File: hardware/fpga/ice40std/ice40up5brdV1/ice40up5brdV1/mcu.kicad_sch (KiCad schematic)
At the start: 10 parts, among them J3 Conn_01x06_Male, J4 Conn_01x04_Male, U5 ATSAMD11D14A-M

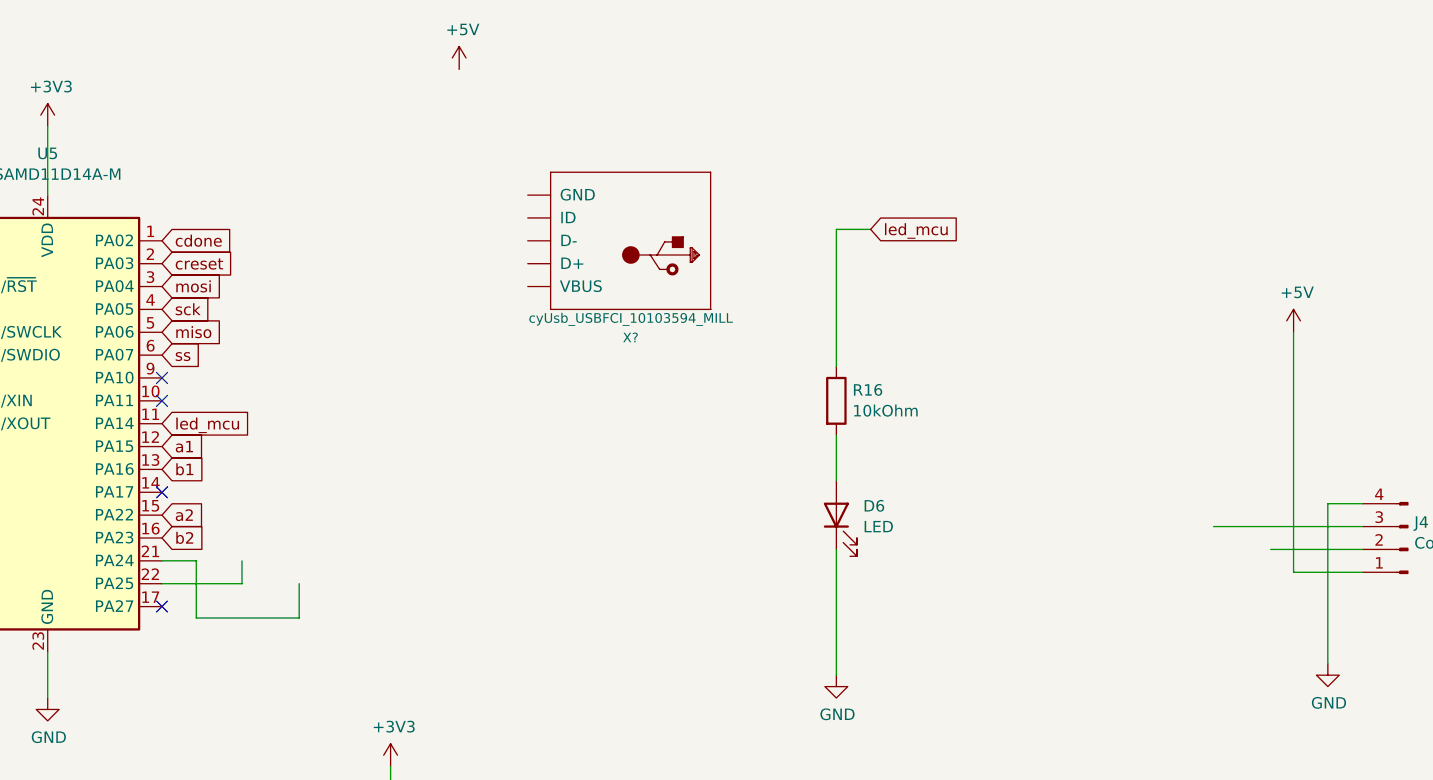
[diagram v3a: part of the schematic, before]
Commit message: started linear regs / Amphenol USB
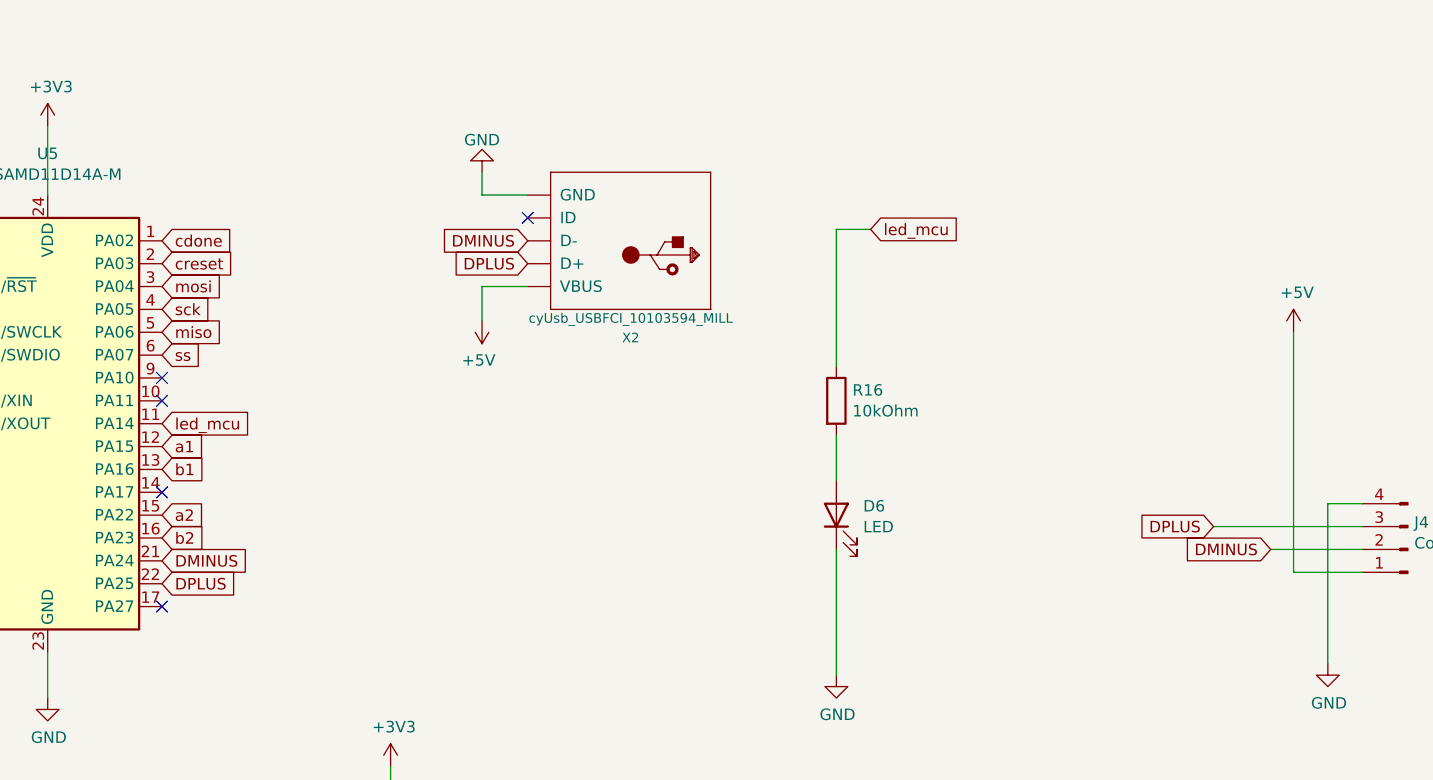
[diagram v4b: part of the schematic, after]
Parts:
- gave numbers to parts that had none: 1
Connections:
- net +5V: now also X2.VBUS
- net GND: now also X2.BASE@1 (GND), X2.BASE@2 (GND), X2.GND, X2.SPRT@1 (GND), X2.SPRT@2 (GND), X2.SPRT@3 (GND), X2.SPRT@4 (GND)
- net DMINUS: now reaches U5.21 (PA24)
- net DMINUS: now also J4.2 (Pin_2), X2.D-
- net DPLUS: now reaches U5.22 (PA25)
- net DPLUS: now also J4.3 (Pin_3), X2.D+
- no-connect marks 4 -> 5
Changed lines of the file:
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@@
   (no_connect (at 88.9 55.88))
   (no_connect (at 88.9 81.28))
+  (no_connect (at 129.54 38.1))
   (wire (pts (xy 106.68 102.87) (xy 114.3 102.87))
     (stroke (width 0) (type default) (color 0 0 0 0))
@@
     (stroke (width 0) (type default) (color 0 0 0 0))
   )
-  (wire (pts (xy 92.71 76.2) (xy 92.71 82.55))
-    (stroke (width 0) (type default) (color 0 0 0 0))
-  )
   (wire (pts (xy 33.02 71.12) (xy 33.02 80.01))
     (stroke (width 0) (type default) (color 0 0 0 0))
@@
     (stroke (width 0) (type default) (color 0 0 0 0))
   )
-  (wire (pts (xy 92.71 82.55) (xy 104.14 82.55))
-    (stroke (width 0) (type default) (color 0 0 0 0))
-  )
   (wire (pts (xy 33.02 58.42) (xy 33.02 63.5))
     (stroke (width 0) (type default) (color 0 0 0 0))
@@
     (stroke (width 0) (type default) (color 0 0 0 0))
   )
-  (wire (pts (xy 88.9 76.2) (xy 92.71 76.2))
+  (wire (pts (xy 124.46 45.72) (xy 129.54 45.72))
     (stroke (width 0) (type default) (color 0 0 0 0))
   )
@@
     (stroke (width 0) (type default) (color 0 0 0 0))
   )
-  (wire (pts (xy 97.79 78.74) (xy 97.79 76.2))
-    (stroke (width 0) (type default) (color 0 0 0 0))
-  )
   (wire (pts (xy 49.53 135.89) (xy 49.53 129.54))
     (stroke (width 0) (type default) (color 0 0 0 0))
@@
     (stroke (width 0) (type default) (color 0 0 0 0))
   )
+  (wire (pts (xy 124.46 33.02) (xy 124.46 35.56))
+    (stroke (width 0) (type default) (color 0 0 0 0))
+  )
+  (wire (pts (xy 124.46 35.56) (xy 129.54 35.56))
+    (stroke (width 0) (type default) (color 0 0 0 0))
+  )
   (wire (pts (xy 46.99 125.73) (xy 40.64 125.73))
     (stroke (width 0) (type default) (color 0 0 0 0))
@@
     (stroke (width 0) (type default) (color 0 0 0 0))
   )
-  (wire (pts (xy 104.14 82.55) (xy 104.14 78.74))
-    (stroke (width 0) (type default) (color 0 0 0 0))
-  )
   (wire (pts (xy 163.83 54.61) (xy 163.83 39.37))
     (stroke (width 0) (type default) (color 0 0 0 0))
   )
+  (wire (pts (xy 124.46 49.53) (xy 124.46 45.72))
+    (stroke (width 0) (type default) (color 0 0 0 0))
+  )
   (wire (pts (xy 27.94 33.02) (xy 29.21 33.02))
     (stroke (width 0) (type default) (color 0 0 0 0))
@@
     (stroke (width 0) (type default) (color 0 0 0 0))
   )
-  (wire (pts (xy 88.9 78.74) (xy 97.79 78.74))
-    (stroke (width 0) (type default) (color 0 0 0 0))
-  )
   (wire (pts (xy 120.65 102.87) (xy 120.65 106.68))
     (stroke (width 0) (type default) (color 0 0 0 0))
@@
     )
   )
+  (global_label "DPLUS" (shape input) (at 129.54 43.18 180) (fields_autoplaced)
+    (effects (font (size 1.27 1.27)) (justify right))
+    (property "Intersheet References" "${INTERSHEET_REFS}" (id 0) (at 121.1077 43.1006 0)
+      (effects (font (size 1.27 1.27)) (justify right) hide)
+    )
+  )
   (global_label "swd_clk" (shape input) (at 40.64 123.19 180) (fields_autoplaced)
     (effects (font (size 1.27 1.27)) (justify right))
@@
     )
   )
+  (global_label "DPLUS" (shape input) (at 205.74 72.39 180) (fields_autoplaced)
+    (effects (font (size 1.27 1.27)) (justify right))
+    (property "Intersheet References" "${INTERSHEET_REFS}" (id 0) (at 197.3077 72.3106 0)
+      (effects (font (size 1.27 1.27)) (justify right) hide)
+    )
+  )
+  (global_label "DMINUS" (shape input) (at 212.09 74.93 180) (fields_autoplaced)
+    (effects (font (size 1.27 1.27)) (justify right))
+    (property "Intersheet References" "${INTERSHEET_REFS}" (id 0) (at 202.5691 74.8506 0)
+      (effects (font (size 1.27 1.27)) (justify right) hide)
+    )
+  )
+  (global_label "DMINUS" (shape input) (at 129.54 40.64 180) (fields_autoplaced)
+    (effects (font (size 1.27 1.27)) (justify right))
+    (property "Intersheet References" "${INTERSHEET_REFS}" (id 0) (at 120.0191 40.5606 0)
+      (effects (font (size 1.27 1.27)) (justify right) hide)
+    )
+  )
   (global_label "b1" (shape input) (at 88.9 66.04 0) (fields_autoplaced)
     (effects (font (size 1.27 1.27)) (justify left))
@@
     )
   )
+  (global_label "DPLUS" (shape input) (at 88.9 78.74 0) (fields_autoplaced)
+    (effects (font (size 1.27 1.27)) (justify left))
+    (property "Intersheet References" "${INTERSHEET_REFS}" (id 0) (at 97.3323 78.8194 0)
+      (effects (font (size 1.27 1.27)) (justify left) hide)
+    )
+  )
   (global_label "led_mcu" (shape input) (at 167.64 39.37 0) (fields_autoplaced)
     (effects (font (size 1.27 1.27)) (justify left))
@@
     (property "Intersheet References" "${INTERSHEET_REFS}" (id 0) (at 0 0 0)
       (effects (font (size 1.27 1.27)) hide)
+    )
+  )
+  (global_label "DMINUS" (shape input) (at 88.9 76.2 0) (fields_autoplaced)
+    (effects (font (size 1.27 1.27)) (justify left))
+    (property "Intersheet References" "${INTERSHEET_REFS}" (id 0) (at 98.4209 76.2794 0)
+      (effects (font (size 1.27 1.27)) (justify left) hide)
     )
   )
@@
     (pin "4")
   )
-  (symbol (lib_id "power:+5V") (at 121.92 21.59 0) (unit 1)
-    (in_bom yes) (on_board yes)
-    (property "Reference" "#PWR?" (id 0) (at 121.92 25.4 0)
-      (effects (font (size 1.27 1.27)) hide)
-    )
-    (property "Value" "+5V" (id 1) (at 122.301 17.1958 0))
-    (property "Footprint" "" (id 2) (at 121.92 21.59 0)
-      (effects (font (size 1.27 1.27)) hide)
-    )
-    (property "Datasheet" "" (id 3) (at 121.92 21.59 0)
+  (symbol (lib_id "power:+5V") (at 124.46 49.53 180) (unit 1)
+    (in_bom yes) (on_board yes)
+    (property "Reference" "#PWR0102" (id 0) (at 124.46 45.72 0)
+      (effects (font (size 1.27 1.27)) hide)
+    )
+    (property "Value" "+5V" (id 1) (at 124.079 53.9242 0))
+    (property "Footprint" "" (id 2) (at 124.46 49.53 0)
+      (effects (font (size 1.27 1.27)) hide)
+    )
+    (property "Datasheet" "" (id 3) (at 124.46 49.53 0)
       (effects (font (size 1.27 1.27)) hide)
     )
@@
   (symbol (lib_id "conne_fci:cyUsb_USBFCI_10103594_MILL") (at 139.7 40.64 180) (unit 1)
     (in_bom yes) (on_board yes) (fields_autoplaced)
-    (property "Reference" "X?" (id 0) (at 140.9827 51.4238 0)
+    (property "Reference" "X2" (id 0) (at 140.9827 51.4238 0)
       (effects (font (size 1.0668 1.0668)))
     )
@@
     (pin "VBUS")
   )
+  (symbol (lib_id "power:GND") (at 124.46 33.02 180) (unit 1)
+    (in_bom yes) (on_board yes) (fields_autoplaced)
+    (property "Reference" "#PWR013" (id 0) (at 124.46 26.67 0)
+      (effects (font (size 1.27 1.27)) hide)
+    )
+    (property "Value" "GND" (id 1) (at 124.46 29.4442 0))
+    (property "Footprint" "" (id 2) (at 124.46 33.02 0)
+      (effects (font (size 1.27 1.27)) hide)
+    )
+    (property "Datasheet" "" (id 3) (at 124.46 33.02 0)
+      (effects (font (size 1.27 1.27)) hide)
+    )
+    (pin "1")
+  )
 )

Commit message: started linear regs / Amphenol USB / layout
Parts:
- removed J4: Conn_01x04_Male, Connector_PinHeader_2.54mm:PinHeader_1x04_P2.54mm_Horizontal, symbol Connector:Conn_01x04_Male
- added J4: Conn_01x02_Male, Connector_PinHeader_2.54mm:PinHeader_1x02_P2.54mm_Horizontal, symbol Connector:Conn_01x02_Male
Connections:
- net +5V: now also J4.2 (Pin_2)
- net GND: now also J4.1 (Pin_1)
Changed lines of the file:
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@@
     (stroke (width 0) (type default) (color 0 0 0 0))
   )
-  (wire (pts (xy 212.09 74.93) (xy 222.25 74.93))
-    (stroke (width 0) (type default) (color 0 0 0 0))
-  )
-  (wire (pts (xy 222.25 69.85) (xy 218.44 69.85))
+  (wire (pts (xy 214.63 80.01) (xy 210.82 80.01))
     (stroke (width 0) (type default) (color 0 0 0 0))
   )
@@
     (stroke (width 0) (type default) (color 0 0 0 0))
   )
-  (wire (pts (xy 205.74 72.39) (xy 222.25 72.39))
-    (stroke (width 0) (type default) (color 0 0 0 0))
-  )
   (wire (pts (xy 106.68 114.3) (xy 106.68 121.92))
     (stroke (width 0) (type default) (color 0 0 0 0))
@@
     (stroke (width 0) (type default) (color 0 0 0 0))
   )
-  (wire (pts (xy 218.44 69.85) (xy 218.44 87.63))
+  (wire (pts (xy 210.82 80.01) (xy 210.82 97.79))
     (stroke (width 0) (type default) (color 0 0 0 0))
   )
@@
   )
   (wire (pts (xy 106.68 121.92) (xy 114.3 121.92))
-    (stroke (width 0) (type default) (color 0 0 0 0))
-  )
-  (wire (pts (xy 214.63 77.47) (xy 222.25 77.47))
     (stroke (width 0) (type default) (color 0 0 0 0))
   )
@@
     )
   )
-  (global_label "DPLUS" (shape input) (at 205.74 72.39 180) (fields_autoplaced)
-    (effects (font (size 1.27 1.27)) (justify right))
-    (property "Intersheet References" "${INTERSHEET_REFS}" (id 0) (at 197.3077 72.3106 0)
-      (effects (font (size 1.27 1.27)) (justify right) hide)
-    )
-  )
-  (global_label "DMINUS" (shape input) (at 212.09 74.93 180) (fields_autoplaced)
-    (effects (font (size 1.27 1.27)) (justify right))
-    (property "Intersheet References" "${INTERSHEET_REFS}" (id 0) (at 202.5691 74.8506 0)
-      (effects (font (size 1.27 1.27)) (justify right) hide)
-    )
-  )
   (global_label "DMINUS" (shape input) (at 129.54 40.64 180) (fields_autoplaced)
     (effects (font (size 1.27 1.27)) (justify right))
@@
     (pin "1")
   )
-  (symbol (lib_id "power:GND") (at 218.44 87.63 0) (unit 1)
-    (in_bom yes) (on_board yes)
-    (property "Reference" "#PWR048" (id 0) (at 218.44 93.98 0)
-      (effects (font (size 1.27 1.27)) hide)
-    )
-    (property "Value" "GND" (id 1) (at 218.567 92.0242 0))
-    (property "Footprint" "" (id 2) (at 218.44 87.63 0)
-      (effects (font (size 1.27 1.27)) hide)
-    )
-    (property "Datasheet" "" (id 3) (at 218.44 87.63 0)
+  (symbol (lib_id "power:GND") (at 210.82 97.79 0) (unit 1)
+    (in_bom yes) (on_board yes)
+    (property "Reference" "#PWR048" (id 0) (at 210.82 104.14 0)
+      (effects (font (size 1.27 1.27)) hide)
+    )
+    (property "Value" "GND" (id 1) (at 210.947 102.1842 0))
+    (property "Footprint" "" (id 2) (at 210.82 97.79 0)
+      (effects (font (size 1.27 1.27)) hide)
+    )
+    (property "Datasheet" "" (id 3) (at 210.82 97.79 0)
       (effects (font (size 1.27 1.27)) hide)
     )
@@
     (pin "1")
   )
-  (symbol (lib_id "Connector:Conn_01x04_Male") (at 227.33 74.93 180) (unit 1)
-    (in_bom yes) (on_board yes)
-    (property "Reference" "J4" (id 0) (at 228.0412 71.9328 0)
-      (effects (font (size 1.27 1.27)) (justify right))
-    )
-    (property "Value" "Conn_01x04_Male" (id 1) (at 228.0412 74.2442 0)
-      (effects (font (size 1.27 1.27)) (justify right))
-    )
-    (property "Footprint" "Connector_PinHeader_2.54mm:PinHeader_1x04_P2.54mm_Horizontal" (id 2) (at 227.33 74.93 0)
-      (effects (font (size 1.27 1.27)) hide)
-    )
-    (property "Datasheet" "~" (id 3) (at 227.33 74.93 0)
-      (effects (font (size 1.27 1.27)) hide)
-    )
-    (pin "1")
-    (pin "2")
-    (pin "3")
-    (pin "4")
-  )
   (symbol (lib_id "power:+5V") (at 124.46 49.53 180) (unit 1)
     (in_bom yes) (on_board yes)
@@
     (pin "1")
   )
+  (symbol (lib_id "Connector:Conn_01x02_Male") (at 219.71 80.01 180) (unit 1)
+    (in_bom yes) (on_board yes) (fields_autoplaced)
+    (property "Reference" "J4" (id 0) (at 220.4212 77.9053 0)
+      (effects (font (size 1.27 1.27)) (justify right))
+    )
+    (property "Value" "Conn_01x02_Male" (id 1) (at 220.4212 80.4422 0)
+      (effects (font (size 1.27 1.27)) (justify right))
+    )
+    (property "Footprint" "Connector_PinHeader_2.54mm:PinHeader_1x02_P2.54mm_Horizontal" (id 2) (at 219.71 80.01 0)
+      (effects (font (size 1.27 1.27)) hide)
+    )
+    (property "Datasheet" "~" (id 3) (at 219.71 80.01 0)
+      (effects (font (size 1.27 1.27)) hide)
+    )
+    (pin "1")
+    (pin "2")
+  )
   (symbol (lib_id "conne_fci:cyUsb_USBFCI_10103594_MILL") (at 139.7 40.64 180) (unit 1)
